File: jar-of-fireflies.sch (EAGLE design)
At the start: 15 parts, among them U1 ATTINY45

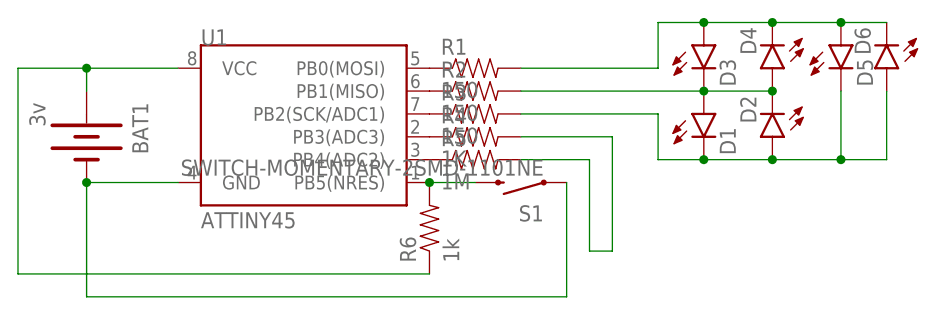
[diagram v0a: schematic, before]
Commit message: Rev 1.1: fixed swapped 1M and 1K resistors, incremented version number.
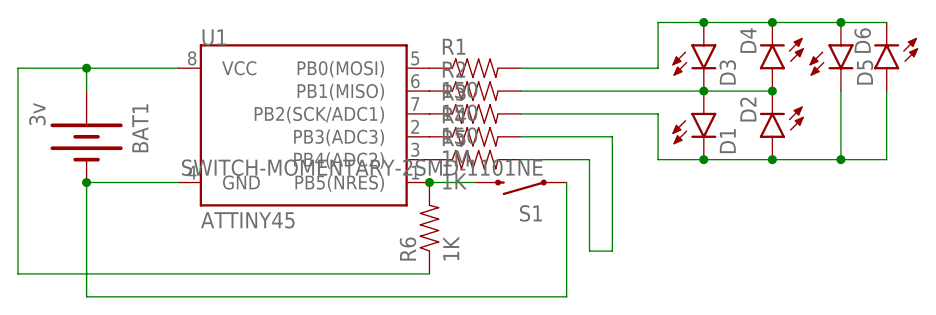
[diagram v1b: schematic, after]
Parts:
- R4: value 1K -> 1M
- R5: value 1M -> 1K
- R6: value 1k -> 1K
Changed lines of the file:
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@@
 <part name="R2" library="SparkFun-Passives" deviceset="RESISTOR" device="PTH-1/4W" value="150"/>
 <part name="R3" library="SparkFun-Passives" deviceset="RESISTOR" device="PTH-1/4W" value="150"/>
-<part name="R4" library="SparkFun-Passives" deviceset="RESISTOR" device="PTH-1/4W" value="1K"/>
-<part name="R5" library="SparkFun-Passives" deviceset="RESISTOR" device="PTH-1/4W" value="1M"/>
+<part name="R4" library="SparkFun-Passives" deviceset="RESISTOR" device="PTH-1/4W" value="1M"/>
+<part name="R5" library="SparkFun-Passives" deviceset="RESISTOR" device="PTH-1/4W" value="1K"/>
 <part name="S1" library="SparkFun-Electromechanical" deviceset="SWITCH-MOMENTARY-2" device="SMD-1101NE" value="SWITCH-MOMENTARY-2SMD-1101NE"/>
-<part name="R6" library="SparkFun-Passives" deviceset="RESISTOR" device="PTH-1/4W" value="1k"/>
+<part name="R6" library="SparkFun-Passives" deviceset="RESISTOR" device="PTH-1/4W" value="1K"/>
 <part name="D1" library="SparkFun-LED" deviceset="LED" device="3MM"/>
 <part name="D2" library="SparkFun-LED" deviceset="LED" device="3MM"/>

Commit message: up to rev 1.2. Gave up on touch sense, replaced with through-hole switch, fewer components!
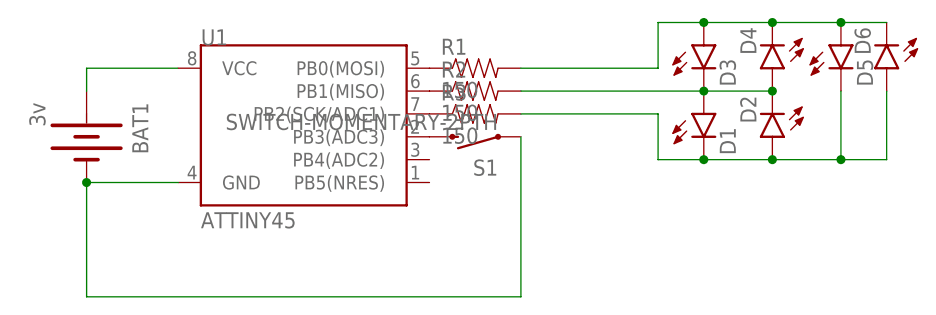
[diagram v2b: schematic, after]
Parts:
- removed R4: 1M, SparkFun-Passives:RESISTORPTH-1/4W
- removed R5, R6: 1K, SparkFun-Passives:RESISTORPTH-1/4W
- S1: value SWITCH-MOMENTARY-2SMD-1101NE -> SWITCH-MOMENTARY-2PTH; device SparkFun-Electromechanical:SWITCH-MOMENTARY-2SMD-1101NE -> SparkFun-Electromechanical:SWITCH-MOMENTARY-2PTH
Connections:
- removed net N$11: R6.2, S1.2, U1.PB5(NRES)
- removed net N$5: R5.1, U1.PB4(ADC2)
- removed net RING: R4.2, R5.2
- net N$4: now also S1.2; no longer R4.1
- net VCC: no longer R6.1
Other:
- moved on the sheet: S1
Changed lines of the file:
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@@
 <part name="R2" library="SparkFun-Passives" deviceset="RESISTOR" device="PTH-1/4W" value="150"/>
 <part name="R3" library="SparkFun-Passives" deviceset="RESISTOR" device="PTH-1/4W" value="150"/>
-<part name="R4" library="SparkFun-Passives" deviceset="RESISTOR" device="PTH-1/4W" value="1M"/>
-<part name="R5" library="SparkFun-Passives" deviceset="RESISTOR" device="PTH-1/4W" value="1K"/>
-<part name="S1" library="SparkFun-Electromechanical" deviceset="SWITCH-MOMENTARY-2" device="SMD-1101NE" value="SWITCH-MOMENTARY-2SMD-1101NE"/>
-<part name="R6" library="SparkFun-Passives" deviceset="RESISTOR" device="PTH-1/4W" value="1K"/>
+<part name="S1" library="SparkFun-Electromechanical" deviceset="SWITCH-MOMENTARY-2" device="PTH" value="SWITCH-MOMENTARY-2PTH"/>
 <part name="D1" library="SparkFun-LED" deviceset="LED" device="3MM"/>
 <part name="D2" library="SparkFun-LED" deviceset="LED" device="3MM"/>
@@
 <instance part="R2" gate="G$1" x="86.36" y="99.06"/>
 <instance part="R3" gate="G$1" x="86.36" y="96.52"/>
-<instance part="R4" gate="G$1" x="86.36" y="93.98"/>
-<instance part="R5" gate="G$1" x="86.36" y="91.44"/>
-<instance part="S1" gate="G$1" x="91.44" y="88.9" rot="R180"/>
-<instance part="R6" gate="G$1" x="81.28" y="83.82" rot="R90"/>
+<instance part="S1" gate="G$1" x="86.36" y="93.98" rot="R180"/>
 <instance part="D1" gate="G$1" x="111.76" y="96.52"/>
 <instance part="D2" gate="G$1" x="119.38" y="93.98" rot="R180"/>
@@
 <pinref part="U1" gate="G$1" pin="PB2(SCK/ADC1)"/>
 <pinref part="R3" gate="G$1" pin="1"/>
-</segment>
-</net>
-<net name="N$4" class="0">
-<segment>
-<pinref part="U1" gate="G$1" pin="PB3(ADC3)"/>
-<pinref part="R4" gate="G$1" pin="1"/>
-</segment>
-</net>
-<net name="N$5" class="0">
-<segment>
-<pinref part="U1" gate="G$1" pin="PB4(ADC2)"/>
-<pinref part="R5" gate="G$1" pin="1"/>
 </segment>
 </net>
@@
 <pinref part="U1" gate="G$1" pin="VCC"/>
 <wire x1="53.34" y1="101.6" x2="43.18" y2="101.6" width="0.1524" layer="91"/>
-<pinref part="R6" gate="G$1" pin="1"/>
-<wire x1="43.18" y1="101.6" x2="35.56" y2="101.6" width="0.1524" layer="91"/>
-<wire x1="81.28" y1="78.74" x2="35.56" y2="78.74" width="0.1524" layer="91"/>
-<wire x1="35.56" y1="78.74" x2="35.56" y2="101.6" width="0.1524" layer="91"/>
 <pinref part="BAT1" gate="G$1" pin="+"/>
 <wire x1="43.18" y1="99.06" x2="43.18" y2="101.6" width="0.1524" layer="91"/>
-<junction x="43.18" y="101.6"/>
 </segment>
 </net>
 <net name="GND" class="0">
 <segment>
-<wire x1="96.52" y1="76.2" x2="43.18" y2="76.2" width="0.1524" layer="91"/>
 <pinref part="U1" gate="G$1" pin="GND"/>
 <wire x1="53.34" y1="88.9" x2="43.18" y2="88.9" width="0.1524" layer="91"/>
+<pinref part="BAT1" gate="G$1" pin="-"/>
 <wire x1="43.18" y1="88.9" x2="43.18" y2="76.2" width="0.1524" layer="91"/>
-<pinref part="BAT1" gate="G$1" pin="-"/>
+<pinref part="S1" gate="G$1" pin="1"/>
+<wire x1="43.18" y1="76.2" x2="91.44" y2="76.2" width="0.1524" layer="91"/>
+<wire x1="91.44" y1="76.2" x2="91.44" y2="93.98" width="0.1524" layer="91"/>
 <junction x="43.18" y="88.9"/>
-<pinref part="S1" gate="G$1" pin="1"/>
-<wire x1="96.52" y1="76.2" x2="96.52" y2="88.9" width="0.1524" layer="91"/>
-</segment>
-</net>
-<net name="N$11" class="0">
-<segment>
-<pinref part="U1" gate="G$1" pin="PB5(NRES)"/>
-<pinref part="R6" gate="G$1" pin="2"/>
-<pinref part="R6" gate="G$1" pin="2"/>
-<pinref part="S1" gate="G$1" pin="2"/>
-<wire x1="86.36" y1="88.9" x2="81.28" y2="88.9" width="0.1524" layer="91"/>
-<junction x="81.28" y="88.9"/>
-</segment>
-</net>
-<net name="RING" class="0">
-<segment>
-<pinref part="R4" gate="G$1" pin="2"/>
-<wire x1="91.44" y1="93.98" x2="101.6" y2="93.98" width="0.1524" layer="91"/>
-<wire x1="101.6" y1="93.98" x2="101.6" y2="81.28" width="0.1524" layer="91"/>
-<wire x1="101.6" y1="81.28" x2="99.06" y2="81.28" width="0.1524" layer="91"/>
-<wire x1="99.06" y1="81.28" x2="99.06" y2="91.44" width="0.1524" layer="91"/>
-<pinref part="R5" gate="G$1" pin="2"/>
-<wire x1="99.06" y1="91.44" x2="91.44" y2="91.44" width="0.1524" layer="91"/>
 </segment>
 </net>
@@
 </segment>
 </net>
+<net name="N$4" class="0">
+<segment>
+<pinref part="U1" gate="G$1" pin="PB3(ADC3)"/>
+<pinref part="S1" gate="G$1" pin="2"/>
+</segment>
+</net>
